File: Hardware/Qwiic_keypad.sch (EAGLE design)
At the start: 25 parts, among them J3 PTH, J6 AVR_SPI_PROG_3X2TESTPOINTS, J7 Keypad, U3 ATTINY84

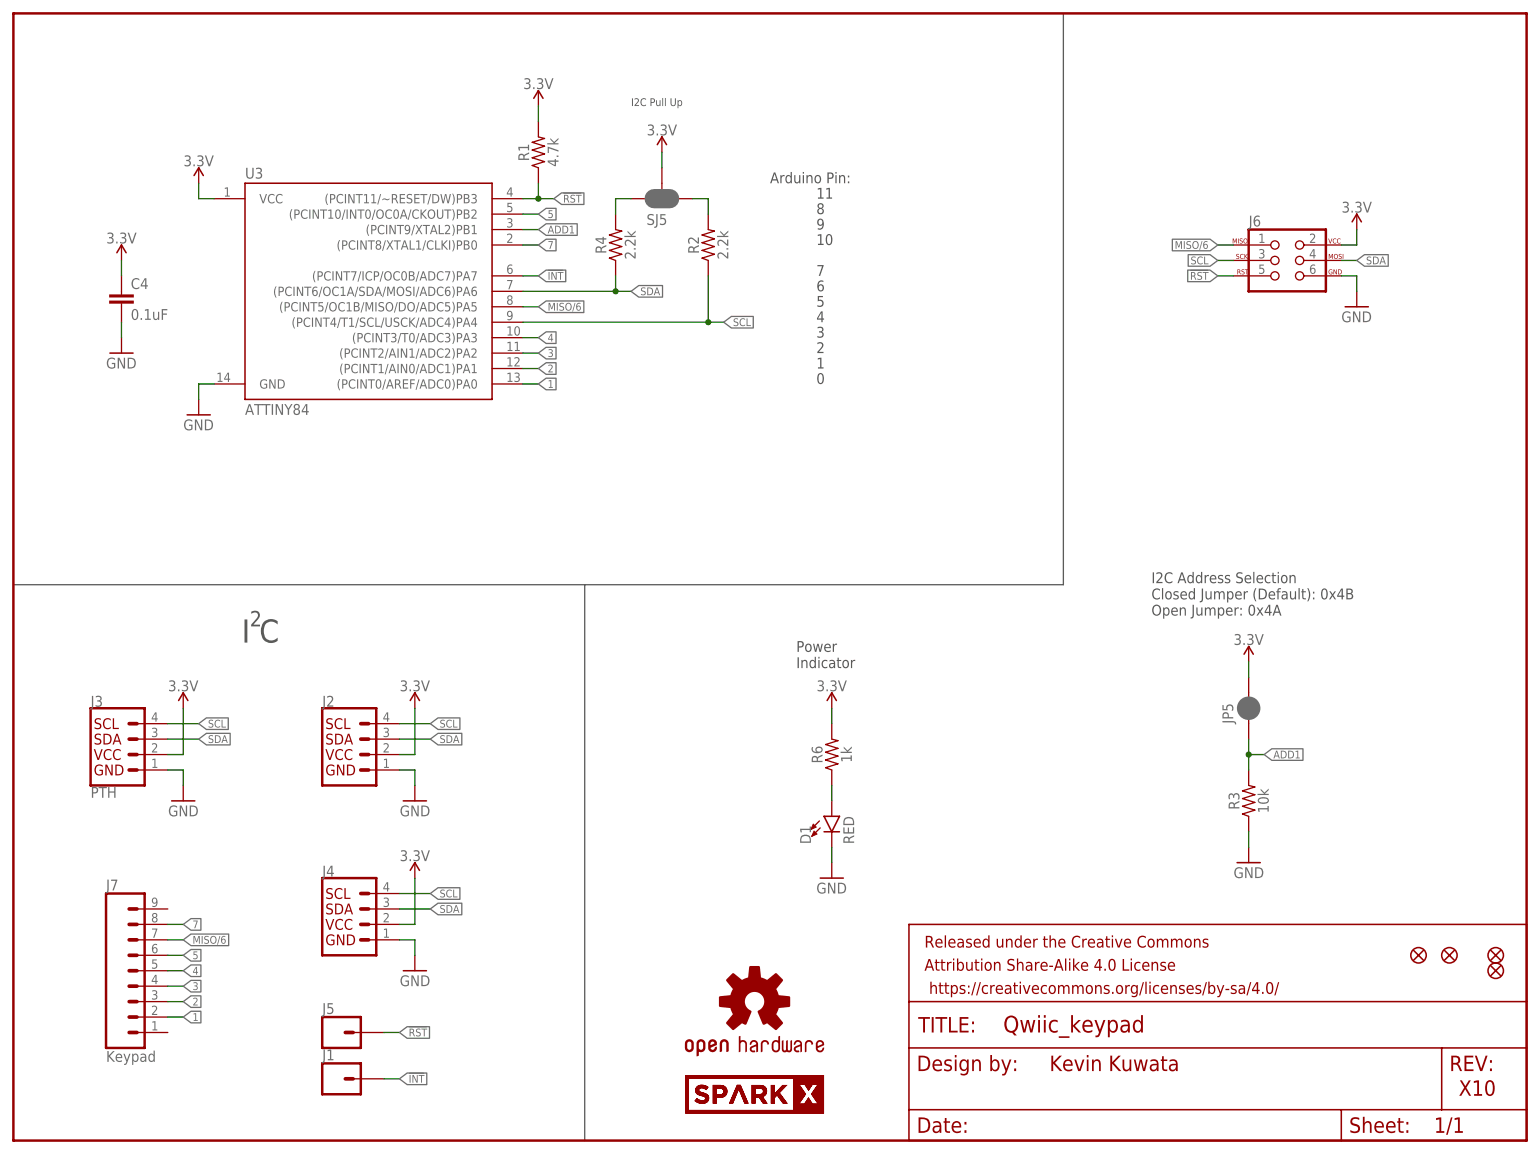
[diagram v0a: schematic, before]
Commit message: Smaller board size.
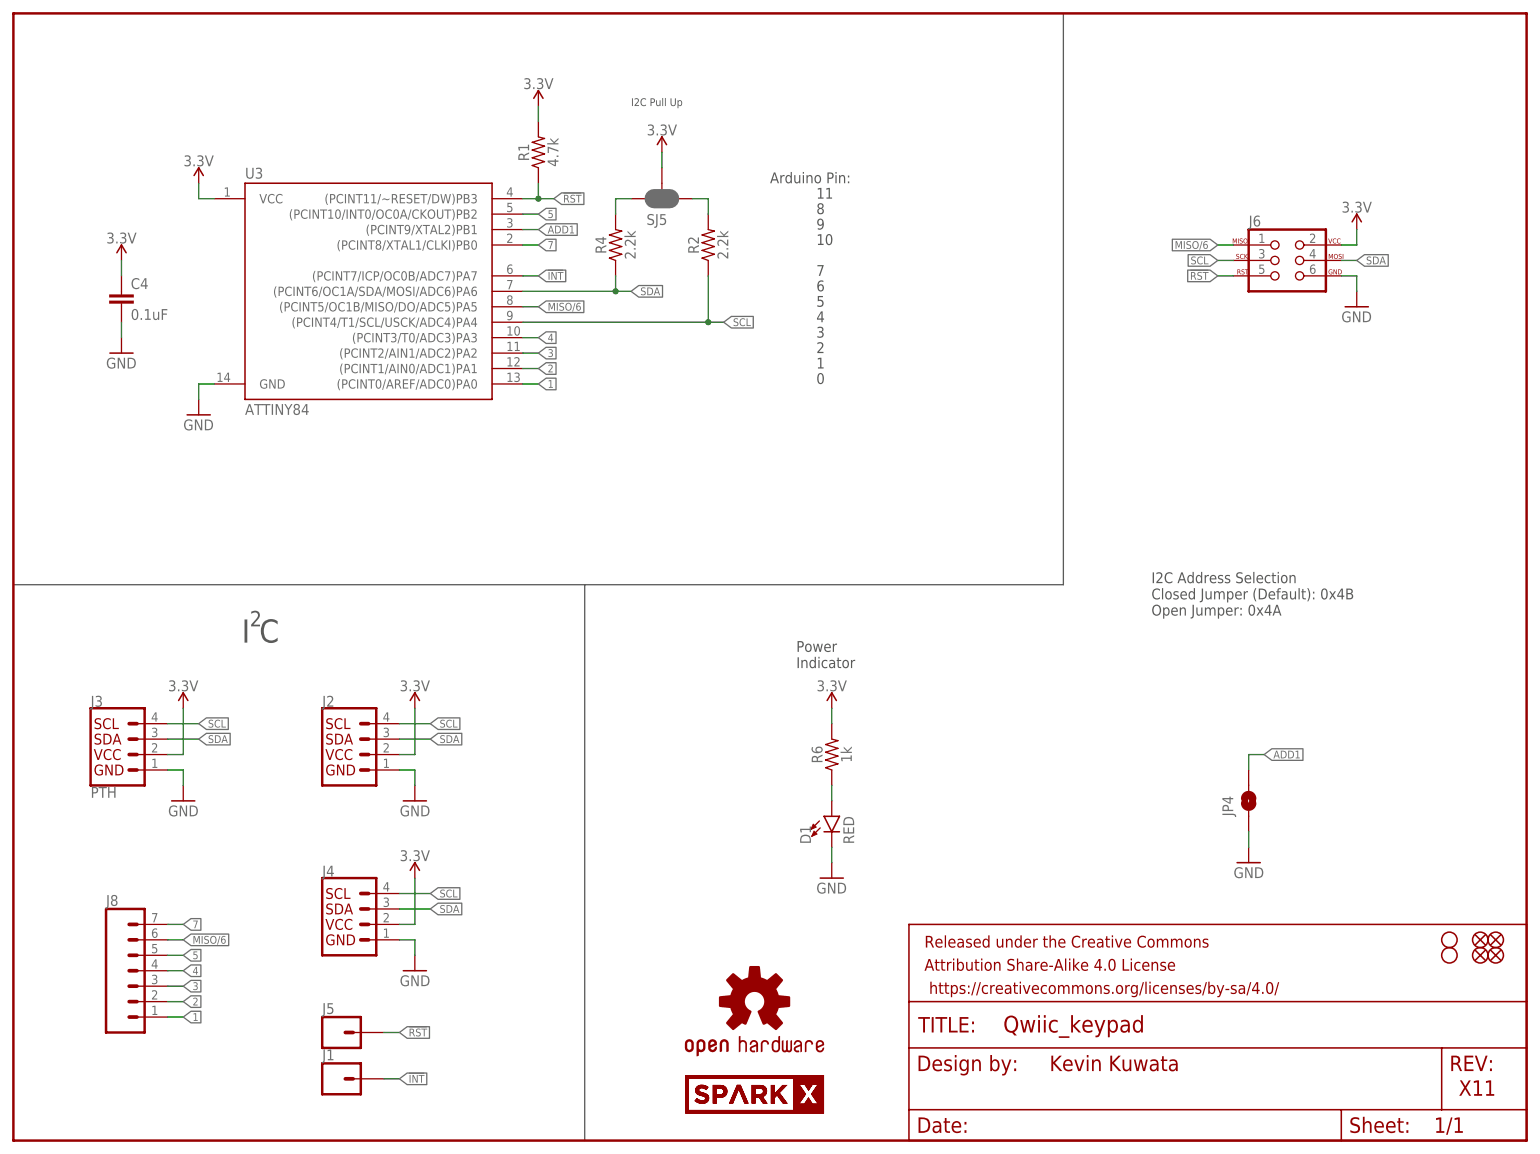
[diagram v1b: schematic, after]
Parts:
- removed J7: Keypad, SparkFun-Connectors:CONN_09NO_SILK
- removed JP5: JUMPER-SMT_2_NC_PASTE_NO-SILK, SparkFun-Jumpers:JUMPER-SMT_2_NC_PASTE_NO-SILK
- removed R3: 10k, SparkFun-Resistors:10KOHM-0603-1/10W-1%
- added H1, H2: STAND-OFF, SparkFun-Hardware:STAND-OFF
- added J8: (no value), SparkFun-Connectors:CONN_07NO_SILK
- added JP4: JUMPER-SMT_2_NO_SILK, SparkFun-Jumpers:JUMPER-SMT_2_NO_SILK
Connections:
- net 1: now also J8.1; no longer J7.2
- net 2: now also J8.2; no longer J7.3
- net 3: now also J8.3; no longer J7.4
- net 3.3V: no longer JP5.2
- net 4: now also J8.4; no longer J7.5
- net 5: now also J8.5; no longer J7.6
- net 7: now also J8.7; no longer J7.8
- net ADD1: now also JP4.2; no longer JP5.1, R3.2
- net GND: now also JP4.1; no longer R3.1
- net MISO/6: now also J8.6; no longer J7.7
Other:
- note added: "X11"
- note removed: "X10"
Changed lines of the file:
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@@
 <part name="SUPPLY1" library="SparkFun-PowerSymbols" deviceset="3.3V" device=""/>
 <part name="J1" library="SparkFun-Connectors" deviceset="CONN_01" device="PTH_NO_SILK_YES_STOP"/>
-<part name="R3" library="SparkFun-Resistors" deviceset="10KOHM" device="-0603-1/10W-1%" value="10k"/>
 <part name="GND2" library="SparkFun" deviceset="GND" device=""/>
-<part name="JP5" library="SparkFun-Jumpers" deviceset="JUMPER-SMT_2_NC_PASTE" device="_NO-SILK"/>
-<part name="SUPPLY3" library="SparkFun-PowerSymbols" deviceset="3.3V" device=""/>
 <part name="U3" library="SparkFun-IC-Microcontroller" deviceset="ATTINY84" device="" value="ATTINY84"/>
 <part name="SUPPLY2" library="SparkFun-PowerSymbols" deviceset="3.3V" device=""/>
@@
 <part name="JP3" library="SparkFun" deviceset="FIDUCIAL" device="UFIDUCIAL"/>
 <part name="J5" library="SparkFun-Connectors" deviceset="CONN_01" device="PTH_NO_SILK_YES_STOP"/>
-<part name="J7" library="SparkFun-Connectors" deviceset="CONN_09" device="NO_SILK" value="Keypad"/>
+<part name="JP4" library="SparkFun-Jumpers" deviceset="JUMPER-SMT_2_NO" device="_SILK" value=""/>
+<part name="H1" library="SparkFun-Hardware" deviceset="STAND-OFF" device=""/>
+<part name="H2" library="SparkFun-Hardware" deviceset="STAND-OFF" device=""/>
+<part name="J8" library="SparkFun-Connectors" deviceset="CONN_07" device="NO_SILK"/>
 </parts>
 <sheets>
@@
 <plain>
 <text x="170.434" y="11.43" size="2.54" layer="94">Kevin Kuwata</text>
-<text x="237.744" y="7.366" size="2.54" layer="94">X10</text>
+<text x="237.744" y="7.366" size="2.54" layer="94">X11</text>
 <text x="40.64" y="83.82" size="3.81" layer="97" align="center">I C</text>
 <text x="39.878" y="85.852" size="2.54" layer="97" align="center">2</text>
@@
 </plain>
 <instances>
-<instance part="JP2" gate="G$1" x="231.14" y="30.48"/>
-<instance part="JP6" gate="G$1" x="236.22" y="30.48"/>
+<instance part="JP2" gate="G$1" x="241.3" y="30.48"/>
+<instance part="JP6" gate="G$1" x="241.3" y="33.02"/>
 <instance part="SUPPLY4" gate="G$1" x="66.04" y="71.12" rot="MR0"/>
 <instance part="SUPPLY5" gate="G$1" x="17.78" y="144.78"/>
@@
 <instance part="SUPPLY1" gate="G$1" x="106.68" y="162.56"/>
 <instance part="J1" gate="G$1" x="53.34" y="10.16"/>
-<instance part="R3" gate="G$1" x="203.2" y="55.88" rot="R90"/>
 <instance part="GND2" gate="1" x="203.2" y="45.72" rot="MR0"/>
-<instance part="JP5" gate="G$1" x="203.2" y="71.12" smashed="yes" rot="R90">
-<attribute name="NAME" x="200.66" y="68.58" size="1.778" layer="95" font="vector" rot="R90"/>
-</instance>
-<instance part="SUPPLY3" gate="G$1" x="203.2" y="78.74" rot="MR0"/>
 <instance part="U3" gate="G$1" x="58.42" y="139.7"/>
 <instance part="SUPPLY2" gate="G$1" x="30.48" y="157.48"/>
@@
 <instance part="D1" gate="G$1" x="134.62" y="53.34"/>
 <instance part="R6" gate="G$1" x="134.62" y="63.5" rot="R90"/>
-<instance part="JP1" gate="G$1" x="243.84" y="30.48"/>
-<instance part="JP3" gate="G$1" x="243.84" y="27.94"/>
+<instance part="JP1" gate="G$1" x="243.84" y="33.02"/>
+<instance part="JP3" gate="G$1" x="243.84" y="30.48"/>
 <instance part="J5" gate="G$1" x="53.34" y="17.78"/>
-<instance part="J7" gate="G$1" x="15.24" y="27.94"/>
+<instance part="JP4" gate="G$1" x="203.2" y="55.88" rot="R90"/>
+<instance part="H1" gate="G$1" x="236.22" y="33.02"/>
+<instance part="H2" gate="G$1" x="236.22" y="30.48"/>
+<instance part="J8" gate="G$1" x="20.32" y="25.4"/>
 </instances>
 <busses>
@@
 </segment>
 <segment>
-<wire x1="203.2" y1="76.2" x2="203.2" y2="78.74" width="0.1524" layer="91"/>
-<pinref part="SUPPLY3" gate="G$1" pin="3.3V"/>
-<pinref part="JP5" gate="G$1" pin="2"/>
-</segment>
-<segment>
 <pinref part="U3" gate="G$1" pin="VCC"/>
 <wire x1="33.02" y1="154.94" x2="30.48" y2="154.94" width="0.1524" layer="91"/>
@@
 </segment>
 <segment>
-<wire x1="203.2" y1="50.8" x2="203.2" y2="48.26" width="0.1524" layer="91"/>
-<pinref part="GND2" gate="1" pin="GND"/>
-<pinref part="R3" gate="G$1" pin="1"/>
-</segment>
-<segment>
 <pinref part="U3" gate="G$1" pin="GND"/>
 <wire x1="33.02" y1="124.46" x2="30.48" y2="124.46" width="0.1524" layer="91"/>
@@
 <pinref part="D1" gate="G$1" pin="C"/>
 </segment>
+<segment>
+<pinref part="GND2" gate="1" pin="GND"/>
+<pinref part="JP4" gate="G$1" pin="1"/>
+<wire x1="203.2" y1="50.8" x2="203.2" y2="48.26" width="0.1524" layer="91"/>
+</segment>
 </net>
 <net name="!INT" class="0">
@@
 <segment>
 <label x="205.74" y="63.5" size="1.27" layer="95" xref="yes"/>
-<pinref part="R3" gate="G$1" pin="2"/>
 <wire x1="203.2" y1="63.5" x2="205.74" y2="63.5" width="0.1524" layer="91"/>
+<pinref part="JP4" gate="G$1" pin="2"/>
 <wire x1="203.2" y1="60.96" x2="203.2" y2="63.5" width="0.1524" layer="91"/>
-<junction x="203.2" y="63.5"/>
-<pinref part="JP5" gate="G$1" pin="1"/>
-<wire x1="203.2" y1="66.04" x2="203.2" y2="63.5" width="0.1524" layer="91"/>
 </segment>
 <segment>
@@
 <wire x1="25.4" y1="27.94" x2="27.94" y2="27.94" width="0.1524" layer="91"/>
 <label x="27.94" y="27.94" size="1.27" layer="95" xref="yes"/>
-<pinref part="J7" gate="G$1" pin="5"/>
+<pinref part="J8" gate="G$1" pin="4"/>
 </segment>
 <segment>
@@
 <wire x1="25.4" y1="25.4" x2="27.94" y2="25.4" width="0.1524" layer="91"/>
 <label x="27.94" y="25.4" size="1.27" layer="95" xref="yes"/>
-<pinref part="J7" gate="G$1" pin="4"/>
+<pinref part="J8" gate="G$1" pin="3"/>
 </segment>
 <segment>
@@
 <wire x1="25.4" y1="22.86" x2="27.94" y2="22.86" width="0.1524" layer="91"/>
 <label x="27.94" y="22.86" size="1.27" layer="95" xref="yes"/>
-<pinref part="J7" gate="G$1" pin="3"/>
+<pinref part="J8" gate="G$1" pin="2"/>
 </segment>
 <segment>
@@
 <wire x1="25.4" y1="20.32" x2="27.94" y2="20.32" width="0.1524" layer="91"/>
 <label x="27.94" y="20.32" size="1.27" layer="95" xref="yes"/>
-<pinref part="J7" gate="G$1" pin="2"/>
+<pinref part="J8" gate="G$1" pin="1"/>
 </segment>
 <segment>
@@
 <wire x1="25.4" y1="33.02" x2="27.94" y2="33.02" width="0.1524" layer="91"/>
 <label x="27.94" y="33.02" size="1.27" layer="95" xref="yes"/>
-<pinref part="J7" gate="G$1" pin="7"/>
+<pinref part="J8" gate="G$1" pin="6"/>
 </segment>
 <segment>
@@
 <wire x1="25.4" y1="35.56" x2="27.94" y2="35.56" width="0.1524" layer="91"/>
 <label x="27.94" y="35.56" size="1.27" layer="95" xref="yes"/>
-<pinref part="J7" gate="G$1" pin="8"/>
+<pinref part="J8" gate="G$1" pin="7"/>
 </segment>
 </net>
@@
 <wire x1="25.4" y1="30.48" x2="27.94" y2="30.48" width="0.1524" layer="91"/>
 <label x="27.94" y="30.48" size="1.27" layer="95" xref="yes"/>
-<pinref part="J7" gate="G$1" pin="6"/>
-</segment>
-</net>
+<pinref part="J8" gate="G$1" pin="5"/>
+</segment>
+</net>

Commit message: Board Revision
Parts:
- removed R4: 2.2k, SparkFun-Resistors:2.2KOHM-0603-1/10W-1%
- added R3: 2.2k, SparkFun-Resistors:2.2KOHM-0603-1/10W-1%
- SJ5: value JUMPER-SMT_3_2-NC_PASTE_SILK -> JUMPER-SMT_3_2-NC_TRACE_SILK; device SparkFun-Jumpers:JUMPER-SMT_3_2-NC_PASTE_SILK -> SparkFun-Jumpers:JUMPER-SMT_3_2-NC_TRACE_SILK
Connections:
- removed net SCL_PU1: R2.2, SJ5.1
- removed net SDA_PU1: R4.2, SJ5.3
- new net N$2: R2.2, SJ5.3
- new net N$3: R3.2, SJ5.1
- net SCL: now also R3.1; no longer R2.1
- net SDA: now also R2.1; no longer R4.1
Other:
- moved on the sheet: R2
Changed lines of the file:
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@@
 <?xml version="1.0" encoding="utf-8"?>
 <!DOCTYPE eagle SYSTEM "eagle.dtd">
-<eagle version="7.7.0">
+<eagle version="9.0.1">
 <drawing>
 <settings>
 <setting alwaysvectorfont="yes"/>
+<setting keepoldvectorfont="yes"/>
 <setting verticaltext="up"/>
 </settings>
@@
 <part name="LOGO1" library="SparkFun-Aesthetics" deviceset="OSHW-LOGO" device="MINI"/>
 <part name="U$1" library="SparkX" deviceset="SPARKX-LOGO" device="3" value="SPARKX-LOGO3"/>
-<part name="R2" library="SparkFun-Resistors" deviceset="2.2KOHM" device="-0603-1/10W-1%" value="2.2k"/>
-<part name="R4" library="SparkFun-Resistors" deviceset="2.2KOHM" device="-0603-1/10W-1%" value="2.2k"/>
-<part name="SJ5" library="SparkFun-Jumpers" deviceset="JUMPER-SMT_3_2-NC_PASTE" device="_SILK" value=""/>
-<part name="SUPPLY1" library="SparkFun-PowerSymbols" deviceset="3.3V" device=""/>
+<part name="SJ5" library="SparkFun-Jumpers" deviceset="JUMPER-SMT_3_2-NC_TRACE" device="_SILK" value=""/>
 <part name="J1" library="SparkFun-Connectors" deviceset="CONN_01" device="PTH_NO_SILK_YES_STOP"/>
 <part name="GND2" library="SparkFun" deviceset="GND" device=""/>
@@
 <part name="H2" library="SparkFun-Hardware" deviceset="STAND-OFF" device=""/>
 <part name="J8" library="SparkFun-Connectors" deviceset="CONN_07" device="NO_SILK"/>
+<part name="R2" library="SparkFun-Resistors" deviceset="2.2KOHM" device="-0603-1/10W-1%" value="2.2k"/>
+<part name="R3" library="SparkFun-Resistors" deviceset="2.2KOHM" device="-0603-1/10W-1%" value="2.2k"/>
+<part name="SUPPLY1" library="SparkFun-PowerSymbols" deviceset="3.3V" device=""/>
 </parts>
 <sheets>
@@
 <text x="128.778" y="77.724" size="1.778" layer="97">Power
 Indicator</text>
-<text x="101.6" y="170.18" size="1.27" layer="97">I2C Pull Up</text>
+<text x="111.76" y="170.18" size="1.27" layer="97" rot="R180">I2C Pull Up</text>
 <wire x1="172.72" y1="185.42" x2="172.72" y2="91.44" width="0.2032" layer="97"/>
 <text x="124.46" y="157.48" size="1.778" layer="97" ratio="15">Arduino Pin:</text>
@@
 <instance part="LOGO1" gate="G$1" x="121.92" y="22.86"/>
 <instance part="U$1" gate="G$1" x="121.92" y="7.62"/>
-<instance part="R2" gate="G$1" x="114.3" y="147.32" rot="R90"/>
-<instance part="R4" gate="G$1" x="99.06" y="147.32" rot="R90"/>
 <instance part="SJ5" gate="G$1" x="106.68" y="154.94" smashed="yes" rot="R270">
 <attribute name="NAME" x="104.14" y="150.622" size="1.778" layer="95" font="vector"/>
 <attribute name="VALUE" x="106.299" y="152.4" size="1.778" layer="96" font="vector" rot="R270" align="top-left"/>
 </instance>
-<instance part="SUPPLY1" gate="G$1" x="106.68" y="162.56"/>
 <instance part="J1" gate="G$1" x="53.34" y="10.16"/>
 <instance part="GND2" gate="1" x="203.2" y="45.72" rot="MR0"/>
@@
 <instance part="H2" gate="G$1" x="236.22" y="30.48"/>
 <instance part="J8" gate="G$1" x="20.32" y="25.4"/>
+<instance part="R2" gate="G$1" x="101.6" y="147.32" rot="R90"/>
+<instance part="R3" gate="G$1" x="111.76" y="147.32" rot="R90"/>
+<instance part="SUPPLY1" gate="G$1" x="106.68" y="162.56"/>
 </instances>
 <busses>
@@
 </segment>
 <segment>
-<wire x1="106.68" y1="160.02" x2="106.68" y2="162.56" width="0.1524" layer="91"/>
-<pinref part="SUPPLY1" gate="G$1" pin="3.3V"/>
-<pinref part="SJ5" gate="G$1" pin="2"/>
-</segment>
-<segment>
 <pinref part="U3" gate="G$1" pin="VCC"/>
 <wire x1="33.02" y1="154.94" x2="30.48" y2="154.94" width="0.1524" layer="91"/>
@@
 <wire x1="134.62" y1="71.12" x2="134.62" y2="68.58" width="0.1524" layer="91"/>
 </segment>
+<segment>
+<wire x1="106.68" y1="160.02" x2="106.68" y2="162.56" width="0.1524" layer="91"/>
+<pinref part="SUPPLY1" gate="G$1" pin="3.3V"/>
+<pinref part="SJ5" gate="G$1" pin="2"/>
+</segment>
 </net>
 <net name="GND" class="0">
@@
 <wire x1="83.82" y1="142.24" x2="86.36" y2="142.24" width="0.1524" layer="91"/>
 <label x="86.36" y="142.24" size="1.27" layer="95" xref="yes"/>
-</segment>
-</net>
-<net name="SCL_PU1" class="0">
-<segment>
-<pinref part="SJ5" gate="G$1" pin="1"/>
-<pinref part="R2" gate="G$1" pin="2"/>
-<wire x1="111.76" y1="154.94" x2="114.3" y2="154.94" width="0.1524" layer="91"/>
-<wire x1="114.3" y1="154.94" x2="114.3" y2="152.4" width="0.1524" layer="91"/>
-</segment>
-</net>
-<net name="SDA_PU1" class="0">
-<segment>
-<pinref part="SJ5" gate="G$1" pin="3"/>
-<pinref part="R4" gate="G$1" pin="2"/>
-<wire x1="101.6" y1="154.94" x2="99.06" y2="154.94" width="0.1524" layer="91"/>
-<wire x1="99.06" y1="154.94" x2="99.06" y2="152.4" width="0.1524" layer="91"/>
 </segment>
 </net>
@@
 <net name="SCL" class="0">
 <segment>
-<pinref part="U3" gate="G$1" pin="(PCINT4/T1/SCL/USCK/ADC4)PA4"/>
-<wire x1="83.82" y1="134.62" x2="114.3" y2="134.62" width="0.1524" layer="91"/>
-<label x="116.84" y="134.62" size="1.27" layer="95" xref="yes"/>
-<pinref part="R2" gate="G$1" pin="1"/>
-<wire x1="114.3" y1="134.62" x2="116.84" y2="134.62" width="0.1524" layer="91"/>
-<wire x1="114.3" y1="142.24" x2="114.3" y2="134.62" width="0.1524" layer="91"/>
-<junction x="114.3" y="134.62"/>
-</segment>
-<segment>
 <pinref part="J6" gate="G$1" pin="3"/>
 <wire x1="200.66" y1="144.78" x2="198.12" y2="144.78" width="0.1524" layer="91"/>
@@
 <label x="68.58" y="40.64" size="1.27" layer="95" rot="MR180" xref="yes"/>
 </segment>
+<segment>
+<pinref part="U3" gate="G$1" pin="(PCINT4/T1/SCL/USCK/ADC4)PA4"/>
+<wire x1="83.82" y1="134.62" x2="111.76" y2="134.62" width="0.1524" layer="91"/>
+<label x="114.3" y="134.62" size="1.27" layer="95" xref="yes"/>
+<pinref part="R3" gate="G$1" pin="1"/>
+<wire x1="111.76" y1="134.62" x2="114.3" y2="134.62" width="0.1524" layer="91"/>
+<wire x1="111.76" y1="142.24" x2="111.76" y2="134.62" width="0.1524" layer="91"/>
+<junction x="111.76" y="134.62"/>
+</segment>
 </net>
 <net name="SDA" class="0">
-<segment>
-<pinref part="U3" gate="G$1" pin="(PCINT6/OC1A/SDA/MOSI/ADC6)PA6"/>
-<wire x1="83.82" y1="139.7" x2="99.06" y2="139.7" width="0.1524" layer="91"/>
-<label x="101.6" y="139.7" size="1.27" layer="95" xref="yes"/>
-<pinref part="R4" gate="G$1" pin="1"/>
-<wire x1="99.06" y1="139.7" x2="101.6" y2="139.7" width="0.1524" layer="91"/>
-<wire x1="99.06" y1="142.24" x2="99.06" y2="139.7" width="0.1524" layer="91"/>
-<junction x="99.06" y="139.7"/>
-</segment>
 <segment>
 <pinref part="J6" gate="G$1" pin="4"/>
@@
 <label x="68.58" y="38.1" size="1.27" layer="95" rot="MR180" xref="yes"/>
 </segment>
-</net>
+<segment>
+<pinref part="U3" gate="G$1" pin="(PCINT6/OC1A/SDA/MOSI/ADC6)PA6"/>
+<wire x1="83.82" y1="139.7" x2="101.6" y2="139.7" width="0.1524" layer="91"/>
+<label x="104.14" y="139.7" size="1.27" layer="95" xref="yes"/>
+<pinref part="R2" gate="G$1" pin="1"/>
+<wire x1="101.6" y1="139.7" x2="104.14" y2="139.7" width="0.1524" layer="91"/>
+<wire x1="101.6" y1="142.24" x2="101.6" y2="139.7" width="0.1524" layer="91"/>
+<junction x="101.6" y="139.7"/>
+</segment>
+</net>
+<net name="N$2" class="0">
+<segment>
+<pinref part="SJ5" gate="G$1" pin="3"/>
+<pinref part="R2" gate="G$1" pin="2"/>
+<wire x1="101.6" y1="154.94" x2="101.6" y2="152.4" width="0.1524" layer="91"/>
+</segment>
+</net>
+<net name="N$3" class="0">
+<segment>
+<pinref part="SJ5" gate="G$1" pin="1"/>
+<pinref part="R3" gate="G$1" pin="2"/>
+<wire x1="111.76" y1="154.94" x2="111.76" y2="152.4" width="0.1524" layer="91"/>
+</segment>
+</net>
